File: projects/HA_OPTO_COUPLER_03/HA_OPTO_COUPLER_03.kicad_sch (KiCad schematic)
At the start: 27 parts, among them J1 TerminalBlock_2pin, J2 TerminalBlock_3pin, J3 TerminalBlock_2pin, J4 TerminalBlock_2pin, J5 TerminalBlock_2pin, Q1 MMBT3904, Q2 MMBT3904, Q3 MMBT3904, T1 HA-OPTO_COUPLER_03, T2 (C)UweHerting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

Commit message: snapshot after cleaning HA_OPTO_COUPLER_03 project
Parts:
- R1, R3, R5: value R -> 15k
- R2, R4, R6: value R -> 200
- T3: value https___github.com_uherting_MyKiCADRep -> github.com/uherting/MyKiCADRep
- T4: value v0.992 -> v0.994
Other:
- note added: "R0.993: Footprint BC817 == MMBT3904"
- note added: "R0.994: added values for resistors"
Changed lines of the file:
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@@
-(kicad_sch (version 20210406) (generator eeschema)
+(kicad_sch (version 20210621) (generator eeschema)
   (paper "A4")
   (title_block
     (title "HA-OPTO_COUPLER_03")
-    (date "2021-04-18")
-    (rev "0.992")
+    (date "2021-08-26")
+    (rev "0.994")
   )
   (junction (at 31.75 27.94) (diameter 0.9144) (color 0 0 0 0))
@@
     (stroke (width 0) (type solid) (color 0 0 0 0))
   )
+  (text "R0.994: added values for resistors" (at 179.07 177.8 0)
+    (effects (font (size 1.27 1.27)) (justify left bottom))
+  )
+  (text "R0.993: Footprint BC817 == MMBT3904" (at 179.07 180.34 0)
+    (effects (font (size 1.27 1.27)) (justify left bottom))
+  )
   (global_label "GPIO_1" (shape input) (at 24.13 105.41 180) (fields_autoplaced)
     (effects (font (size 1.27 1.27)) (justify right))
@@
   )
   (symbol (lib_id "UH_HA:https___github.com_uherting_MyKiCADRep") (at 236.22 152.4 0) (unit 1)
-    (in_bom yes) (on_board yes) (fields_autoplaced)
-    (property "Reference" "T3" (id 0) (at 237.49 151.7649 0)
-      (effects (font (size 1.27 1.27)) (justify left))
-    )
-    (property "Value" "https___github.com_uherting_MyKiCADRep" (id 1) (at 236.22 154.94 0)
-      (effects (font (size 1.27 1.27)) hide)
-    )
+    (in_bom yes) (on_board yes)
+    (property "Reference" "T3" (id 0) (at 237.49 151.1299 0)
+      (effects (font (size 1.27 1.27)) (justify left))
+    )
+    (property "Value" "github.com{slash}uherting{slash}MyKiCADRep" (id 1) (at 254 153.67 0))
     (property "Footprint" "UH_HA:GithubLink_UH" (id 2) (at 237.49 157.48 0)
       (effects (font (size 1.27 1.27)) hide)
     )
-    (property "Datasheet" "https://github.com/uherting/MyKiCADRep" (id 3) (at 237.49 154.3049 0)
-      (effects (font (size 1.27 1.27)) (justify left))
+    (property "Datasheet" "uherting.MyKiCADRep @ GitHub" (id 3) (at 237.49 153.6699 0)
+      (effects (font (size 1.27 1.27)) (justify left) hide)
     )
   )
@@
       (effects (font (size 1.27 1.27)) (justify left))
     )
-    (property "Value" "v0.992" (id 1) (at 236.855 161.163 0)
+    (property "Value" "v0.994" (id 1) (at 236.855 161.163 0)
       (effects (font (size 1.27 1.27)) (justify left))
     )
@@
     (in_bom yes) (on_board yes)
     (property "Reference" "R1" (id 0) (at 30.48 103.378 90))
-    (property "Value" "R" (id 1) (at 30.48 105.41 90))
+    (property "Value" "15k" (id 1) (at 30.48 107.95 90))
     (property "Footprint" "Resistor_SMD:R_0805_2012Metric_Pad1.20x1.40mm_HandSolder" (id 2) (at 30.48 107.188 90)
       (effects (font (size 1.27 1.27)) hide)
@@
     (in_bom yes) (on_board yes)
     (property "Reference" "R2" (id 0) (at 42.418 80.01 90))
-    (property "Value" "R" (id 1) (at 44.45 80.01 90))
+    (property "Value" "200" (id 1) (at 46.99 80.01 90))
     (property "Footprint" "Resistor_SMD:R_0805_2012Metric_Pad1.20x1.40mm_HandSolder" (id 2) (at 46.228 80.01 90)
       (effects (font (size 1.27 1.27)) hide)
@@
     (in_bom yes) (on_board yes)
     (property "Reference" "R3" (id 0) (at 121.92 103.378 90))
-    (property "Value" "R" (id 1) (at 121.92 105.41 90))
+    (property "Value" "15k" (id 1) (at 121.92 107.95 90))
     (property "Footprint" "Resistor_SMD:R_0805_2012Metric_Pad1.20x1.40mm_HandSolder" (id 2) (at 121.92 107.188 90)
       (effects (font (size 1.27 1.27)) hide)
@@
     (in_bom yes) (on_board yes)
     (property "Reference" "R4" (id 0) (at 133.858 80.01 90))
-    (property "Value" "R" (id 1) (at 135.89 80.01 90))
+    (property "Value" "200" (id 1) (at 138.43 80.01 90))
     (property "Footprint" "Resistor_SMD:R_0805_2012Metric_Pad1.20x1.40mm_HandSolder" (id 2) (at 137.668 80.01 90)
       (effects (font (size 1.27 1.27)) hide)
@@
     (in_bom yes) (on_board yes)
     (property "Reference" "R5" (id 0) (at 214.63 103.378 90))
-    (property "Value" "R" (id 1) (at 214.63 105.41 90))
+    (property "Value" "15k" (id 1) (at 214.63 107.95 90))
     (property "Footprint" "Resistor_SMD:R_0805_2012Metric_Pad1.20x1.40mm_HandSolder" (id 2) (at 214.63 107.188 90)
       (effects (font (size 1.27 1.27)) hide)
@@
     (in_bom yes) (on_board yes)
     (property "Reference" "R6" (id 0) (at 226.568 80.01 90))
-    (property "Value" "R" (id 1) (at 228.6 80.01 90))
+    (property "Value" "200" (id 1) (at 231.14 80.01 90))
     (property "Footprint" "Resistor_SMD:R_0805_2012Metric_Pad1.20x1.40mm_HandSolder" (id 2) (at 230.378 80.01 90)
       (effects (font (size 1.27 1.27)) hide)
@@
       (effects (font (size 1.27 1.27)) (justify right))
     )
-    (property "Value" "TerminalBlock_2pin" (id 1) (at 53.34 31.1149 90)
-      (effects (font (size 1.27 1.27)) (justify right) hide)
+    (property "Value" "TerminalBlock_2pin" (id 1) (at 53.34 38.7349 0)
+      (effects (font (size 1.27 1.27)) (justify right))
     )
     (property "Footprint" "UH_HA:Term_Block_1x2_P5mm" (id 2) (at 45.72 33.02 0)
@@
     )
     (path "/9cf420cf-2ff3-4678-8afb-c7970a4ac43d"
-      (reference "R1") (unit 1) (value "R") (footprint "Resistor_SMD:R_0805_2012Metric_Pad1.20x1.40mm_HandSolder")
+      (reference "R1") (unit 1) (value "15k") (footprint "Resistor_SMD:R_0805_2012Metric_Pad1.20x1.40mm_HandSolder")
     )
     (path "/67811992-e1a1-4368-8aa2-6cfa6ae5cc74"
-      (reference "R2") (unit 1) (value "R") (footprint "Resistor_SMD:R_0805_2012Metric_Pad1.20x1.40mm_HandSolder")
+      (reference "R2") (unit 1) (value "200") (footprint "Resistor_SMD:R_0805_2012Metric_Pad1.20x1.40mm_HandSolder")
     )
     (path "/15e05f3c-bb85-4bd0-ae61-696b2fb161ed"
-      (reference "R3") (unit 1) (value "R") (footprint "Resistor_SMD:R_0805_2012Metric_Pad1.20x1.40mm_HandSolder")
+      (reference "R3") (unit 1) (value "15k") (footprint "Resistor_SMD:R_0805_2012Metric_Pad1.20x1.40mm_HandSolder")
     )
     (path "/3e807842-f325-4ff9-a071-138cb1abbbde"
-      (reference "R4") (unit 1) (value "R") (footprint "Resistor_SMD:R_0805_2012Metric_Pad1.20x1.40mm_HandSolder")
+      (reference "R4") (unit 1) (value "200") (footprint "Resistor_SMD:R_0805_2012Metric_Pad1.20x1.40mm_HandSolder")
     )
     (path "/caa63a1e-8058-4dd2-bc99-66700844109c"
-      (reference "R5") (unit 1) (value "R") (footprint "Resistor_SMD:R_0805_2012Metric_Pad1.20x1.40mm_HandSolder")
+      (reference "R5") (unit 1) (value "15k") (footprint "Resistor_SMD:R_0805_2012Metric_Pad1.20x1.40mm_HandSolder")
     )
     (path "/04a8e636-9292-4dca-9bfd-2396b4eb6521"
-      (reference "R6") (unit 1) (value "R") (footprint "Resistor_SMD:R_0805_2012Metric_Pad1.20x1.40mm_HandSolder")
+      (reference "R6") (unit 1) (value "200") (footprint "Resistor_SMD:R_0805_2012Metric_Pad1.20x1.40mm_HandSolder")
     )
     (path "/ef122801-95d3-44b6-bb4a-f547e7e15b85"
@@
     )
     (path "/df5a76cd-0c42-4f7b-a35a-c4687cbe96ce"
-      (reference "T3") (unit 1) (value "https___github.com_uherting_MyKiCADRep") (footprint "UH_HA:GithubLink_UH")
+      (reference "T3") (unit 1) (value "github.com{slash}uherting{slash}MyKiCADRep") (footprint "UH_HA:GithubLink_UH")
     )
     (path "/3accd7f6-2913-4cf7-8f4c-9e796dbc15f0"
-      (reference "T4") (unit 1) (value "v0.992") (footprint "UH_HA:PCB_Version")
+      (reference "T4") (unit 1) (value "v0.994") (footprint "UH_HA:PCB_Version")
     )
     (path "/06fcd9b0-d4c4-4e3d-8069-42db06a687df"

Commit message: HA_OPTO_COUPLER_03: changed values for R1, R3, R5
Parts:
- R1, R3, R5: value 15k -> 12k
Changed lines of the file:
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@@
     (in_bom yes) (on_board yes)
     (property "Reference" "R1" (id 0) (at 30.48 103.378 90))
-    (property "Value" "15k" (id 1) (at 30.48 107.95 90))
+    (property "Value" "12k" (id 1) (at 30.48 107.95 90))
     (property "Footprint" "Resistor_SMD:R_0805_2012Metric_Pad1.20x1.40mm_HandSolder" (id 2) (at 30.48 107.188 90)
       (effects (font (size 1.27 1.27)) hide)
@@
     (in_bom yes) (on_board yes)
     (property "Reference" "R3" (id 0) (at 121.92 103.378 90))
-    (property "Value" "15k" (id 1) (at 121.92 107.95 90))
+    (property "Value" "12k" (id 1) (at 121.92 107.95 90))
     (property "Footprint" "Resistor_SMD:R_0805_2012Metric_Pad1.20x1.40mm_HandSolder" (id 2) (at 121.92 107.188 90)
       (effects (font (size 1.27 1.27)) hide)
@@
     (in_bom yes) (on_board yes)
     (property "Reference" "R5" (id 0) (at 214.63 103.378 90))
-    (property "Value" "15k" (id 1) (at 214.63 107.95 90))
+    (property "Value" "12k" (id 1) (at 214.63 107.95 90))
     (property "Footprint" "Resistor_SMD:R_0805_2012Metric_Pad1.20x1.40mm_HandSolder" (id 2) (at 214.63 107.188 90)
       (effects (font (size 1.27 1.27)) hide)
@@
     )
     (path "/9cf420cf-2ff3-4678-8afb-c7970a4ac43d"
-      (reference "R1") (unit 1) (value "15k") (footprint "Resistor_SMD:R_0805_2012Metric_Pad1.20x1.40mm_HandSolder")
+      (reference "R1") (unit 1) (value "12k") (footprint "Resistor_SMD:R_0805_2012Metric_Pad1.20x1.40mm_HandSolder")
     )
     (path "/67811992-e1a1-4368-8aa2-6cfa6ae5cc74"
@@
     )
     (path "/15e05f3c-bb85-4bd0-ae61-696b2fb161ed"
-      (reference "R3") (unit 1) (value "15k") (footprint "Resistor_SMD:R_0805_2012Metric_Pad1.20x1.40mm_HandSolder")
+      (reference "R3") (unit 1) (value "12k") (footprint "Resistor_SMD:R_0805_2012Metric_Pad1.20x1.40mm_HandSolder")
     )
     (path "/3e807842-f325-4ff9-a071-138cb1abbbde"
@@
     )
     (path "/caa63a1e-8058-4dd2-bc99-66700844109c"
-      (reference "R5") (unit 1) (value "15k") (footprint "Resistor_SMD:R_0805_2012Metric_Pad1.20x1.40mm_HandSolder")
+      (reference "R5") (unit 1) (value "12k") (footprint "Resistor_SMD:R_0805_2012Metric_Pad1.20x1.40mm_HandSolder")
     )
     (path "/04a8e636-9292-4dca-9bfd-2396b4eb6521"

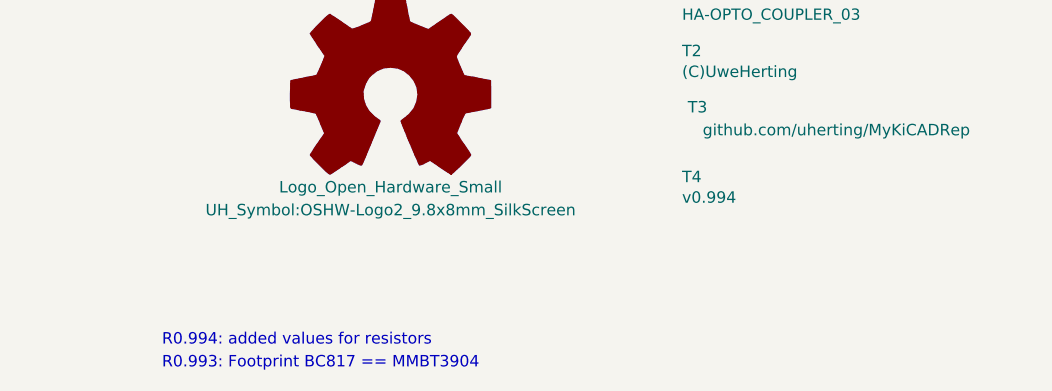
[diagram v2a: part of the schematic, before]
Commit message: added description for solder jumpers
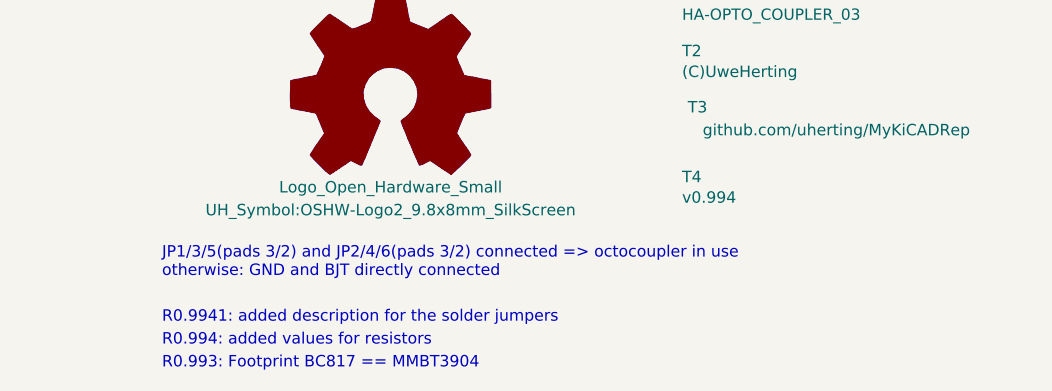
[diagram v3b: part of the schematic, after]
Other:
- note added: "JP1/3/5(pads 3/2) and JP2/4/6(pads 3/2) connected => octocoupler in use otherwise: GND and BJT directly connected"
- note added: "R0.9941: added description for the solder jumpers"
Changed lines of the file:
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@@
   (title_block
     (title "HA-OPTO_COUPLER_03")
-    (date "2021-08-26")
-    (rev "0.994")
+    (date "2021-09-18")
+    (rev "0.9941")
   )
   (junction (at 31.75 27.94) (diameter 0.9144) (color 0 0 0 0))
@@
     (stroke (width 0) (type solid) (color 0 0 0 0))
   )
+  (text "JP1/3/5(pads 3/2) and JP2/4/6(pads 3/2) connected => octocoupler in use\notherwise: GND and BJT directly connected"
+    (at 179.07 170.18 0)
+    (effects (font (size 1.27 1.27)) (justify left bottom))
+  )
+  (text "R0.9941: added description for the solder jumpers" (at 179.07 175.26 0)
+    (effects (font (size 1.27 1.27)) (justify left bottom))
+  )
   (text "R0.994: added values for resistors" (at 179.07 177.8 0)
